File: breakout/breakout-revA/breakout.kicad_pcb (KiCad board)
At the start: 8 copper layers, 127 x 76.2 mm, 244 parts, among them J300 Breakout Connector, J301 Breakout Connector, P1 Conn_01x03, P2 Conn_01x03, P3 Conn_01x03, Q1 MMBT3906-7-F, Q10 MMBT3904-TP, Q11 MMBT3906-7-F, Q12 MMBT3904-TP, Q13 MMBT3906-7-F, Q14 MMBT3904-TP, Q15 MMBT3906-7-F, Q16 MMBT3904-TP, Q17 MMBT3906-7-F, Q18 MMBT3904-TP, Q19 MMBT3906-7-F, Q2 MMBT3906-7-F, Q20 MMBT3904-TP, Q21 MMBT3906-7-F, Q22 MMBT3904-TP, Q23 MMBT3904-TP, Q3 MMBT3906-7-F, Q4 MMBT3906-7-F, Q5 MMBT3906-7-F, Q6 MMBT3904-TP, Q7 MMBT3906-7-F, Q8 MMBT3904-TP, Q9 MMBT3906-7-F, SW1 A6SN-5104, SW2 PTS810 SJS 250 SMTR LFS, SW3 PTS810 SJS 250 SMTR LFS, SW4 PTS810 SJS 250 SMTR LFS

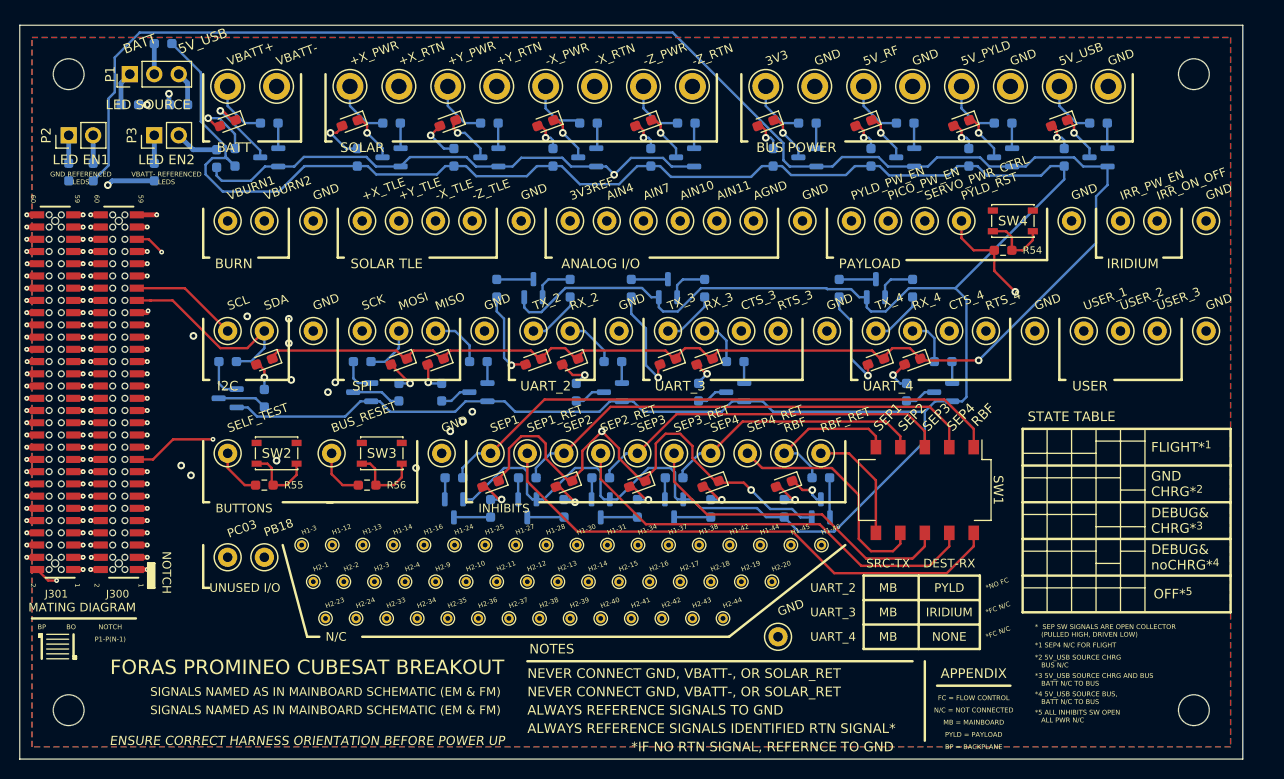
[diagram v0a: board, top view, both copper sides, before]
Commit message: updated silk screen, bom, and sub J301.
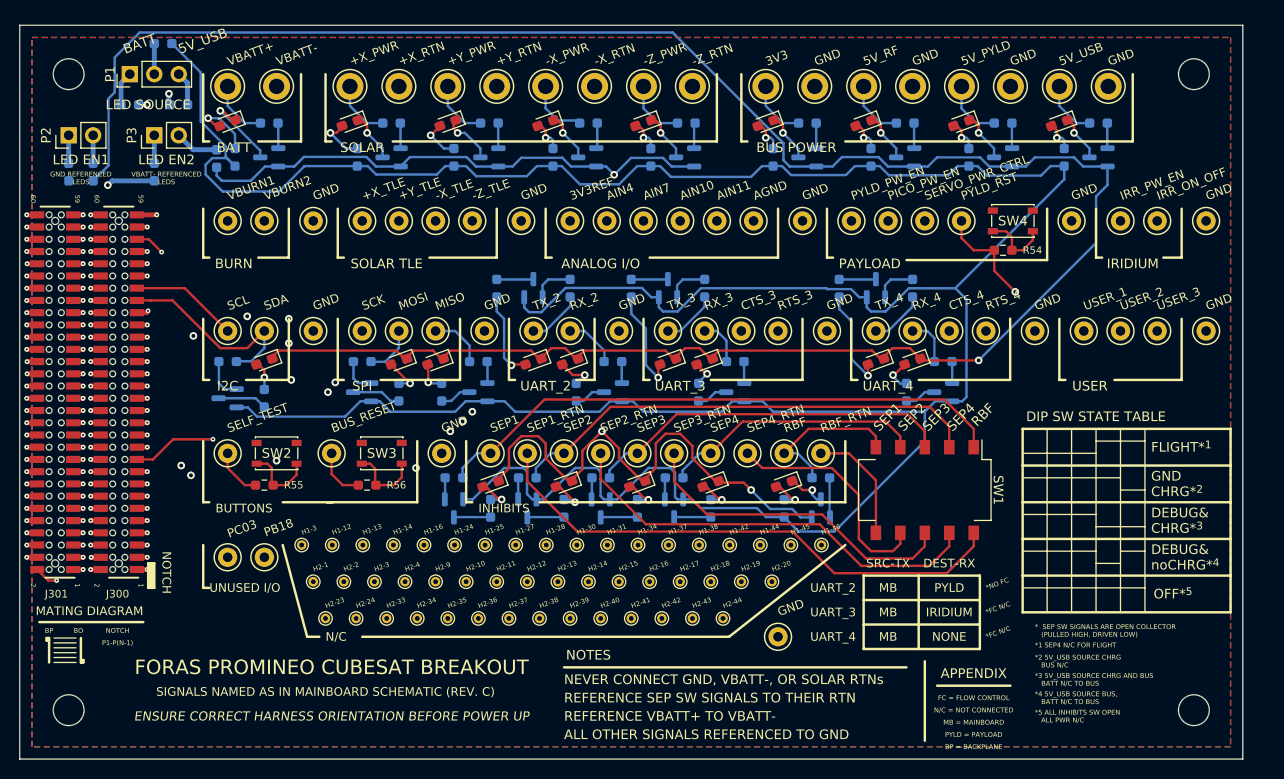
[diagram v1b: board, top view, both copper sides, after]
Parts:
- TP105: value RBF_RET -> RBF_RTN
- TP118: value SEP4_RET -> SEP4_RTN
- TP28: value SEP3_RET -> SEP3_RTN
- TP58: value SEP1_RET -> SEP1_RTN
- TP88: value SEP2_RET -> SEP2_RTN
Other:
- board text added: "ALL OTHER SIGNALS REFERENCED TO GND"
- board text added: "DIP SW STATE TABLE"
- board text added: "NEVER CONNECT GND, VBATT-, OR SOLAR RTNs"
- board text added: "REFERENCE SEP SW SIGNALS TO THEIR RTN"
- board text added: "REFERENCE VBATT+ TO VBATT-"
- board text added: "SIGNALS NAMED AS IN MAINBOARD SCHEMATIC (REV. C)"
- board text removed: "*IF NO RTN SIGNAL, REFERNCE TO GND"
- board text removed: "ALWAYS REFERENCE SIGNALS IDENTIFIED RTN SIGNAL*"
- board text removed: "ALWAYS REFERENCE SIGNALS TO GND"
- board text removed: "NEVER CONNECT GND, VBATT-, OR SOLAR_RET"
- board text removed: "SIGNALS NAMED AS IN MAINBOARD SCHEMATIC (EM & FM)"
- board text removed: "STATE TABLE"
